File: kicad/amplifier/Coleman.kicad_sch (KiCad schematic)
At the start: 0 parts

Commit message: kicad work
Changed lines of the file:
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@@
 (kicad_sch (version 20230121) (generator eeschema)
   (paper "A4")
-  (bus (pts (xy 148.59 73.66) (xy 148.59 78.74))
+  (wire (pts (xy 152.4 72.39) (xy 154.94 72.39))
     (stroke (width 0) (type default))
   )
-  (hierarchical_label "F+" (shape output) (at 147.32 73.66 0) (fields_autoplaced)
+  (wire (pts (xy 154.94 81.28) (xy 153.67 81.28))
+    (stroke (width 0) (type default))
+  )
+  (wire (pts (xy 148.59 78.74) (xy 153.67 78.74))
+    (stroke (width 0) (type default))
+  )
+  (wire (pts (xy 152.4 73.66) (xy 152.4 72.39))
+    (stroke (width 0) (type default))
+  )
+  (wire (pts (xy 147.32 73.66) (xy 152.4 73.66))
+    (stroke (width 0) (type default))
+  )
+  (wire (pts (xy 153.67 81.28) (xy 153.67 78.74))
+    (stroke (width 0) (type default))
+  )
+  (wire (pts (xy 154.94 72.39) (xy 154.94 81.28))
+    (stroke (width 0) (type default))
+  )
+  (hierarchical_label "F+" (shape passive) (at 147.32 73.66 0) (fields_autoplaced)
     (effects (font (size 1.27 1.27)) (justify left))
   )
-  (hierarchical_label "F-" (shape output) (at 147.32 78.74 0) (fields_autoplaced)
+  (hierarchical_label "F-" (shape passive) (at 148.59 78.74 0) (fields_autoplaced)
     (effects (font (size 1.27 1.27)) (justify left))
   )

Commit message: PSU stuff
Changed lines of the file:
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@@
 (kicad_sch (version 20230121) (generator eeschema)
   (paper "A4")
+  (wire (pts (xy 143.51 92.71) (xy 143.51 99.06))
+    (stroke (width 0) (type default))
+  )
+  (wire (pts (xy 147.32 92.71) (xy 143.51 92.71))
+    (stroke (width 0) (type default))
+  )
   (wire (pts (xy 152.4 72.39) (xy 154.94 72.39))
     (stroke (width 0) (type default))
@@
     (stroke (width 0) (type default))
   )
+  (wire (pts (xy 143.51 99.06) (xy 147.32 99.06))
+    (stroke (width 0) (type default))
+  )
   (wire (pts (xy 153.67 81.28) (xy 153.67 78.74))
     (stroke (width 0) (type default))
@@
     (effects (font (size 1.27 1.27)) (justify left))
   )
+  (hierarchical_label "+DC" (shape input) (at 147.32 92.71 0) (fields_autoplaced)
+    (effects (font (size 1.27 1.27)) (justify left))
+  )
+  (hierarchical_label "-DC" (shape input) (at 147.32 99.06 0) (fields_autoplaced)
+    (effects (font (size 1.27 1.27)) (justify left))
+  )

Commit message: coleman
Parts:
- added C1, C2: 100u, symbol Device:C_Polarized
- added C3: 10000u, Capacitor_THT:CP_Radial_D25.0mm_P10.00mm_SnapIn, symbol Device:C_Polarized
- added C6: 330u, symbol Device:C_Polarized
- added C9: 100n, symbol Device:C
- added Q1, Q2: TIP122, Package_TO_SOT_THT:TO-220-3_Vertical, symbol Transistor_BJT:TIP122
- added Q8: 2N5551, symbol Simulation_SPICE:NPN
- added R1: 330, symbol Device:R
- added R19, R21, R3: 1k, symbol Device:R
- added R2: 47k, symbol Device:R
- added R23, R25, R26: 150, symbol Device:R
- added R27: 0.68 2W, symbol Device:R
- added RV3: 500, symbol Device:R_Potentiometer
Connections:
- net +DC: now also C2.1, C3.1, Q2.2 (C), R19.1, R3.1
- net F+: now also Q2.3 (E)
- new net: Q2.1 (B), R1.1
- new net: C1.1, R1.2, R2.1, R3.2
- new net: C9.1, Q8.1 (C), R21.2, R25.1
- new net: C9.2, Q8.2 (B), R26.1, RV3.3
- new net: Q1.3 (E), R26.2, R27.1
- new net: C6.1, R19.2, R21.1
- new net: R23.2, RV3.1, RV3.2
- new net: Q1.1 (B), R25.2
- new net -DC: C1.2, C2.2, C3.2, C6.2, Q8.3 (E), R2.2, R23.1, R27.2
- new net F-: Q1.2 (C)
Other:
- note added: "See http://audiophilediyer.com/dht-filament-regulator"

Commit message: 801 filament supply
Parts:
- removed C6: 330u, symbol Device:C_Polarized
- removed C9: 100n, symbol Device:C
- removed Q8: 2N5551, symbol Simulation_SPICE:NPN
- removed R21: 1k, symbol Device:R
- removed R26: 150, symbol Device:R
- added C6: 220n, Capacitor_THT:C_Rect_L26.5mm_W10.5mm_P22.50mm_MKS4, symbol Device:C
- added D3: 15V, Diode_THT:D_DO-34_SOD68_P7.62mm_Horizontal, symbol Device:D_Zener
- added Q11: IXTP6N50D2, Package_TO_SOT_THT:TO-220-3_Vertical, symbol stax_ccs:10M90S
- added Q13: BC550, Package_TO_SOT_THT:TO-92_Inline, symbol Transistor_BJT:BC550
- added Q15, Q19: LND150, symbol Simulation_SPICE:NMOS
- added Q8: STP55NF06L, Package_TO_SOT_THT:TO-220-3_Vertical, symbol Transistor_FET_Other:DN2540N5-G
- added R28: 4.7M, Resistor_THT:R_Axial_DIN0207_L6.3mm_D2.5mm_P10.16mm_Horizontal, symbol Device:R
- added R30: 50, Resistor_THT:R_Axial_DIN0207_L6.3mm_D2.5mm_P10.16mm_Horizontal, symbol Device:R
- added R34, R35, R38: 1k, Resistor_THT:R_Axial_DIN0207_L6.3mm_D2.5mm_P10.16mm_Horizontal, symbol Device:R
- added R43: 2.5k, Resistor_THT:R_Axial_DIN0207_L6.3mm_D2.5mm_P10.16mm_Horizontal, symbol Device:R
- added RV5: 5k, symbol Device:R_Potentiometer
- R25: value 150 -> 100k
- R27: value 0.68 2W -> 0.68
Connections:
- net -DC is gone; now on an unnamed net: C1.2, C2.2, C3.2, R2.2, R23.1, R27.2
- net +DC: now also Q11.2 (P), Q15.1 (D); no longer C2.1, C3.1, Q2.2 (C), R19.1, R3.1
- net at R25.1: now also Q13.3 (E)
- net at RV3.3: now also Q1.3 (E), R27.1
- net at R19.2: now also C2.1, C3.1, Q2.2 (C), R3.1
- net at R23.2, RV3.1: no longer RV3.2
- net at R25.2: now also RV3.2, Q13.2 (B); no longer Q1.1 (B)
- net F+: no longer names the net of Q2.3 (E)
- net F-: no longer names the net of Q1.2 (C)
- new net: C6.1, D3.1 (K), Q8.1 (G), R28.1
- new net: D3.2 (A), Q8.3 (S), R30.1, R34.2
- new net: Q15.2 (G), R35.1
- new net: Q15.3 (S), Q19.1 (D)
- new net: Q19.2 (G), R38.1
- new net: Q19.3 (S), R35.2, RV5.1
- new net: R28.2, R38.2, R43.1, RV5.2, RV5.3
- new net: Q1.1 (B), Q13.1 (C), R19.1
- new net: Q11.3 (N), Q8.2 (D)
- new net: Q11.1 (G), R34.1
- new net FIL_OUT: C6.2, R30.2
- new net GND: R43.2
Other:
- note added: "1.25 A"
- note added: "Adjust potentiometer to desired CCS current / filament voltage"
- note added: "Inspired by Rod Coleman DHT Filament Regulator and Ale Moglia Gyrator"
- moved on the sheet: C1, C2, C3, Q1, Q2, R1, R2, R23, R27, R3, RV3

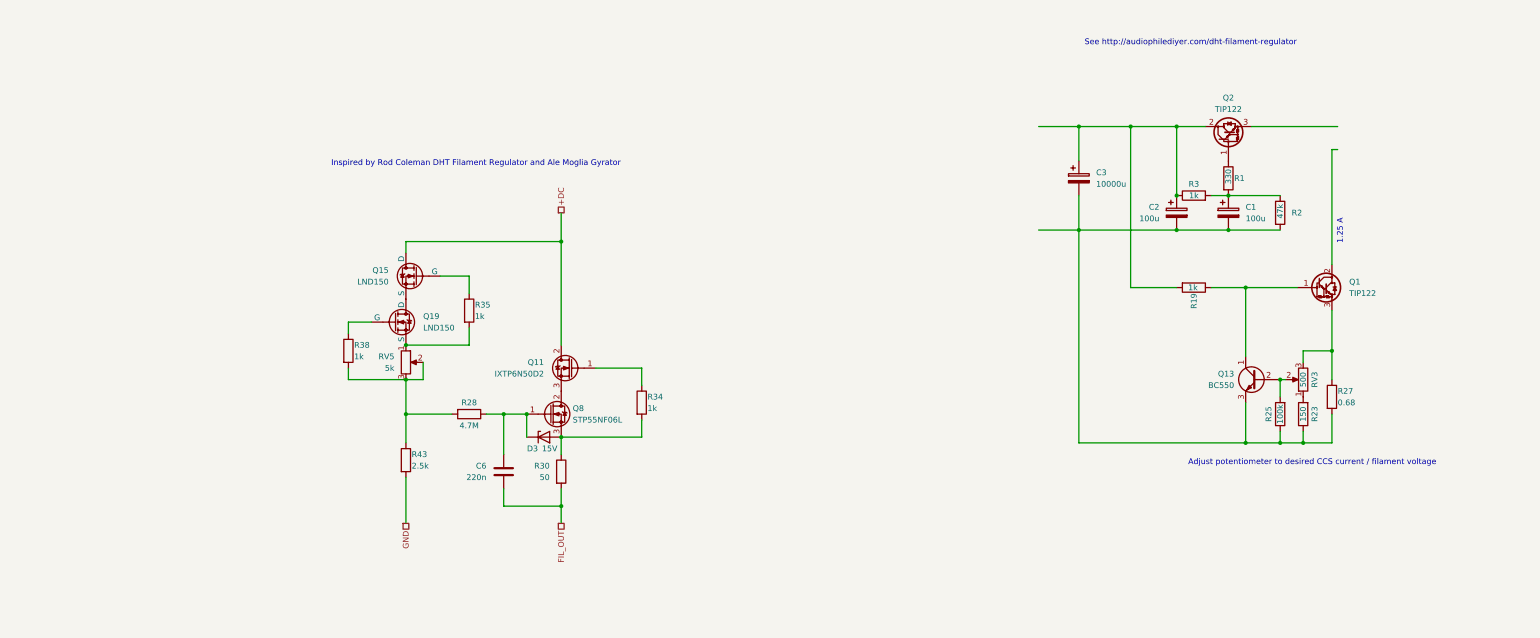
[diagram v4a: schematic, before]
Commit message: modified Colemand DHT filament regulator with negative filament referenced to GND
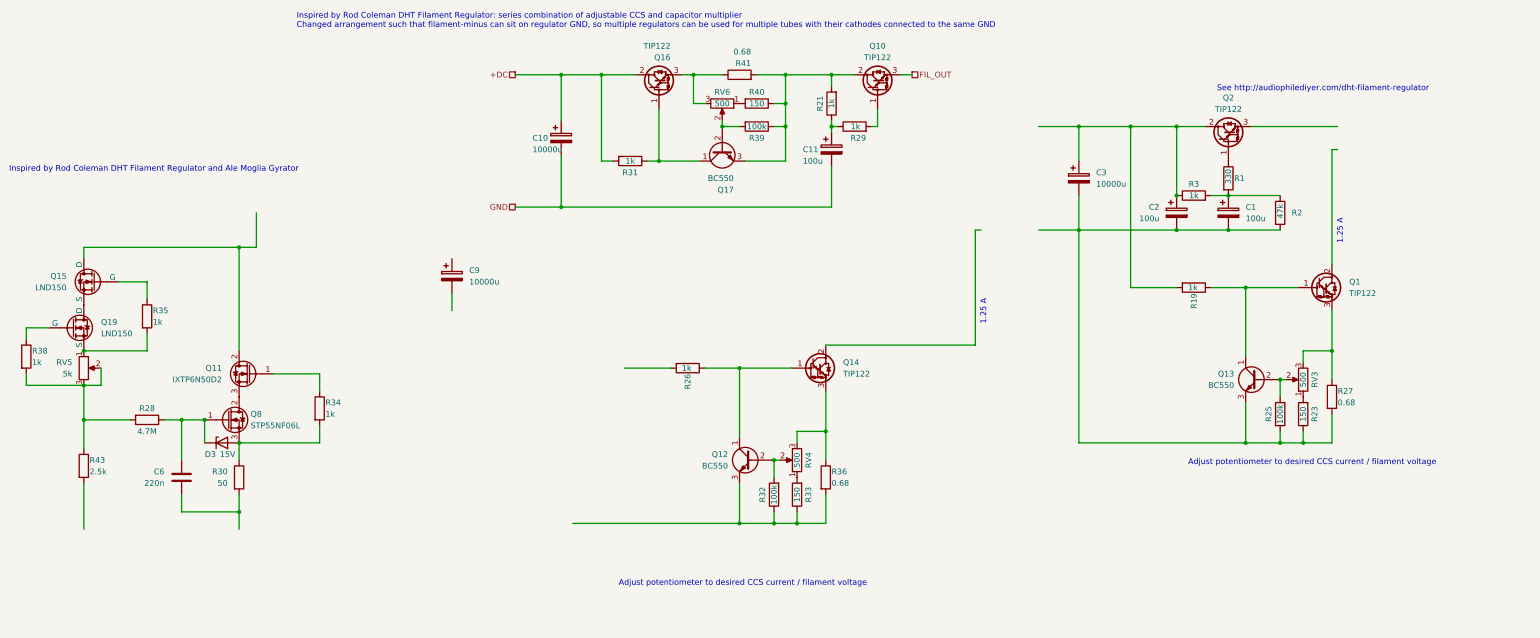
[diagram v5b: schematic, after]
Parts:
- added C10: 10000u, symbol Device:C_Polarized
- added C11: 100u, symbol Device:C_Polarized
- added C9: 10000u, Capacitor_THT:CP_Radial_D25.0mm_P10.00mm_SnapIn, symbol Device:C_Polarized
- added Q10, Q14, Q16: TIP122, Package_TO_SOT_THT:TO-220-3_Vertical, symbol Transistor_BJT:TIP122
- added Q12, Q17: BC550, Package_TO_SOT_THT:TO-92_Inline, symbol Transistor_BJT:BC550
- added R21, R26, R29, R31: 1k, symbol Device:R
- added R32, R39: 100k, symbol Device:R
- added R33, R40: 150, symbol Device:R
- added R36, R41: 0.68, symbol Device:R
- added RV4, RV6: 500, symbol Device:R_Potentiometer
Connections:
- net +DC: now also C10.1, Q16.2 (C), R31.2; no longer Q11.2 (P), Q15.1 (D)
- net FIL_OUT: now also Q10.3 (E); no longer C6.2, R30.2
- net GND: now also C10.2, C11.2; no longer R43.2
- new net: Q16.1 (B), Q17.1 (C), R31.1
- new net: Q17.2 (B), R39.2, RV6.2
- new net: Q10.2 (C), Q17.3 (E), R21.2, R39.1, R40.1, R41.2
- new net: C6.2, R30.2
- new net: Q11.2 (P), Q15.1 (D)
- new net: Q12.1 (C), Q14.1 (B), R26.1
- new net: Q12.2 (B), R32.2, RV4.2
- new net: Q12.3 (E), R32.1, R33.1, R36.2
- new net: R40.2, RV6.1
- new net: Q16.3 (E), R41.1, RV6.3
- new net: C11.1, R21.1, R29.1
- new net: Q10.1 (B), R29.2
- new net: Q14.3 (E), R36.1, RV4.3
- new net: R33.2, RV4.1
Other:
- note added: "Inspired by Rod Coleman DHT Filament Regulator: series combination of adjustable CCS and capacitor multiplier Changed arrangement such that filament-minus can sit on regulator GND, so multiple regulators can be used for multiple tubes with their cathodes connected to the same GND"
- moved on the sheet: C6, D3, Q11, Q15, Q19, Q8, R28, R30, R34, R35, R38, R43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

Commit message: DHT fil reg
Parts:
- removed C1, C11, C2: 100u, symbol Device:C_Polarized
- removed C3, C9: 10000u, Capacitor_THT:CP_Radial_D25.0mm_P10.00mm_SnapIn, symbol Device:C_Polarized
- removed C6: 220n, Capacitor_THT:C_Rect_L26.5mm_W10.5mm_P22.50mm_MKS4, symbol Device:C
- removed D3: 15V, Diode_THT:D_DO-34_SOD68_P7.62mm_Horizontal, symbol Device:D_Zener
- removed Q1, Q10, Q14, Q16, Q2: TIP122, Package_TO_SOT_THT:TO-220-3_Vertical, symbol Transistor_BJT:TIP122
- removed Q11: IXTP6N50D2, Package_TO_SOT_THT:TO-220-3_Vertical, symbol stax_ccs:10M90S
- removed Q12, Q13, Q17: BC550, Package_TO_SOT_THT:TO-92_Inline, symbol Transistor_BJT:BC550
- removed Q15, Q19: LND150, symbol Simulation_SPICE:NMOS
- removed Q8: STP55NF06L, Package_TO_SOT_THT:TO-220-3_Vertical, symbol Transistor_FET_Other:DN2540N5-G
- removed R1: 330, symbol Device:R
- removed R2: 47k, symbol Device:R
- removed R27, R36: 0.68, symbol Device:R
- removed R28: 4.7M, Resistor_THT:R_Axial_DIN0207_L6.3mm_D2.5mm_P10.16mm_Horizontal, symbol Device:R
- removed R3, R31: 1k, symbol Device:R
- removed R30: 50, Resistor_THT:R_Axial_DIN0207_L6.3mm_D2.5mm_P10.16mm_Horizontal, symbol Device:R
- removed R32, R39: 100k, symbol Device:R
- removed R33, R40: 150, symbol Device:R
- removed R34, R35, R38: 1k, Resistor_THT:R_Axial_DIN0207_L6.3mm_D2.5mm_P10.16mm_Horizontal, symbol Device:R
- removed R43: 2.5k, Resistor_THT:R_Axial_DIN0207_L6.3mm_D2.5mm_P10.16mm_Horizontal, symbol Device:R
- removed RV4, RV6: 500, symbol Device:R_Potentiometer
- removed RV5: 5k, symbol Device:R_Potentiometer
- added C11, C5: 5u, symbol Device:C
- added Q10, Q18, Q7, Q8: STP55NF06L, Package_TO_SOT_THT:TO-220-3_Vertical, symbol Simulation_SPICE:NMOS
- added R20: 1k, symbol Device:R
- added R22, R42: 5k, symbol Device:R
- added R24, R44: 1.3R 3W, Resistor_THT:R_Axial_DIN0617_L17.0mm_D6.0mm_P25.40mm_Horizontal, symbol Device:R
- added R45: 100k, symbol Device:R
- added R46: 500, symbol Device:R
- added RV7: 100, symbol Device:R_Potentiometer
- added TH1: CL-110, Varistor:RV_Disc_D12mm_W4.3mm_P7.5mm, symbol Device:Thermistor_NTC
- added U3, U4: LM4041LP-ADJ, Package_TO_SOT_THT:TO-92_Inline, symbol Reference_Voltage:LM4041LP-ADJ
- R19, R21: value 1k -> 1.5M
- R23: value 150 -> 1k
- R25: value 100k -> 500
- R26: value 1k -> 100k
- R41: value 0.68 -> 1k
- RV3: value 500 -> 100
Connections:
- net +DC is gone; now on an unnamed net: C10.1
- net GND is gone; now on net FIL1_OUT: C10.2
- net at R19.2: now also R21.2, Q10.1 (D), Q7.1 (D), TH1.2
- net at R23.1: now also Q8.2 (G); no longer R25.1
- net at R41.2: now also R42.2, U3.2 (K); no longer R21.2
- net FIL1_OUT: now reaches R26.1
- net FIL1_OUT: now also R25.1, C11.2, C5.2, R24.2, R44.2, R45.1, R46.1, U3.3 (A), U4.3 (A)
- net at R26.2: now also RV3.2, U4.1 (FB)
- net at R25.2: now also RV3.1; no longer RV3.2
- net at R41.1: now also Q18.2 (G)
- net at R21.1, R29.1: now also C11.1
- net at R29.2: now also Q10.2 (G)
- net at R19.1: now also C5.1, R20.1
- net at R23.2: now also R22.2, U4.2 (K); no longer RV3.1
- net at RV3.3: now also Q8.3 (S), R24.1
- new net: R45.2, RV7.2, U3.1 (FB)
- new net: Q10.3 (S), Q18.1 (D), R42.1
- new net: Q7.3 (S), Q8.1 (D), R22.1
- new net: Q18.3 (S), R44.1, RV7.3
- new net: Q7.2 (G), R20.2
- new net: R46.2, RV7.1
- new net +RAW_15VDC: TH1.1
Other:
- note added: "1.225V"
- note added: "CCS"
- note added: "Gyrator"
- note added: "Inspired by Rod Coleman DHT Filament Regulator: (for discussion: https://wtfamps.com/2018/10/03/diy-dht-filament-strategies) - Filament driven by high-impedance source (CCS) - Gyrator for DC voltage smoothing Published versions of Coleman DHT Filament regulator cannot be operated from same raw DC supply because the Gyrator and CCS sit on opposite ends of each filament, and one end of each filamen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"
- note added: "from SMPS"
- note removed: "1.25 A"
- note removed: "Adjust potentiometer to desired CCS current / filament voltage"
- note removed: "Inspired by Rod Coleman DHT Filament Regulator and Ale Moglia Gyrator"
- note removed: "Inspired by Rod Coleman DHT Filament Regulator: series combination of adjustable CCS and capacitor multiplier Changed arrangement such that filament-minus can sit on regulator GND, so multiple regulators can be used for multiple tubes with their cathodes connected to the same GND"
- note removed: "See http://audiophilediyer.com/dht-filament-regulator"
- moved on the sheet: C10, R21, R29

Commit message: various
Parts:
- renumbered C5 to C10, C10 to C8, C11 to C9, Q7 to Q10, Q18 to Q11, Q8 to Q12, Q10 to Q9, R21 to R28, R19 to R29, R29 to R30, R20 to R31, R42 to R32, R22 to R33, R41 to R34, R23 to R35, R44 to R36, R24 to R37, R46 to R38, R45 to R39, R25 to R40, R26 to R41, RV7 to RV3, RV3 to RV4, U3 to U5, U4 to U6
